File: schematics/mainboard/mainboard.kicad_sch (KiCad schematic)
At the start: 85 parts, among them J1 ICSP, J10 Conn_AGauge, J11 Conn_SAS, J2 USB_B_Micro, J3 DEALON DC-S050-200, J4 PWR_SELECT, J5 Conn_Joy1, J6 Conn_Joy2, J7 Conn_Throttle, J8 Conn_DGauges, J9 Conn_LCD, Q2 BC849, U1 ATmega2560-16A, U2 FT232RL, U3 USBLC6-2P6, U4 AIP78M05, U5 L9110, U6 74HC595, U7 74HC595, U8 74HC165, U9 74HC165, Y1 16Mhz

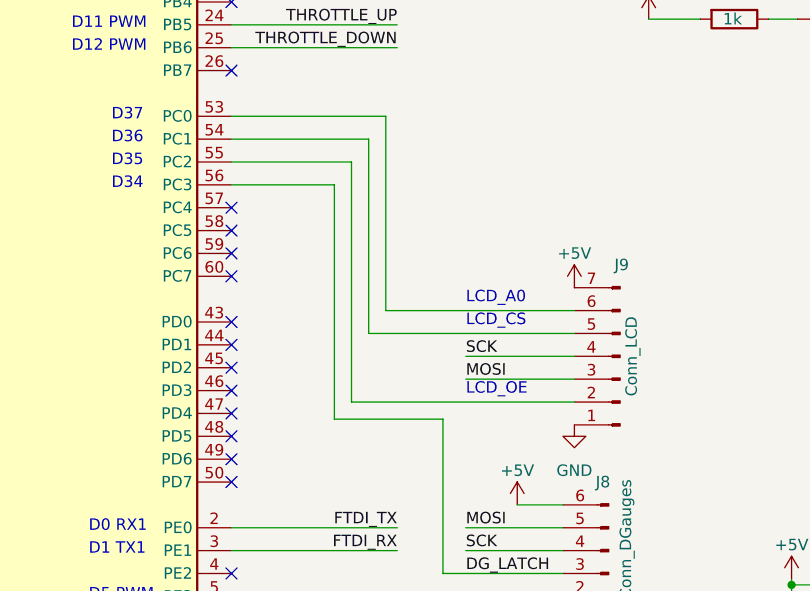
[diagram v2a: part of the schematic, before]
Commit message: SCH: LCD => removed MB OE connection, now pulled to 3.3, always ON
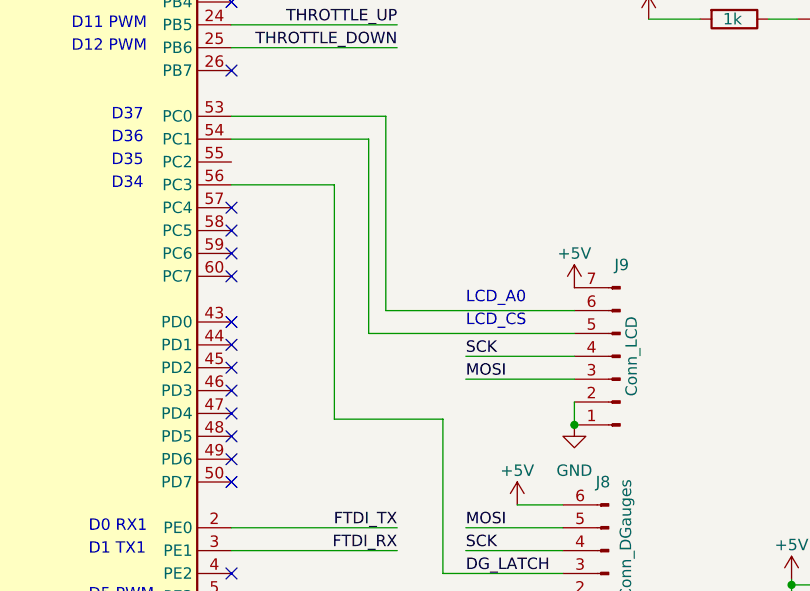
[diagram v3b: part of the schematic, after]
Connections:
- net GND: now also J9.2 (Pin_2)
- net at U1.55 (PC2): no longer J9.2 (Pin_2)
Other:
- note removed: "LCD_OE"
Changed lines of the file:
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@@
   (junction (at 245.745 269.24) (diameter 0) (color 0 0 0 0)
+  )
+  (junction (at 328.295 185.42) (diameter 0) (color 0 0 0 0)
   )
   (junction (at 341.63 218.44) (diameter 0) (color 0 0 0 0)
@@
     (stroke (width 0) (type default))
   )
+  (wire (pts (xy 328.295 182.88) (xy 328.295 185.42))
+    (stroke (width 0) (type default))
+  )
   (wire (pts (xy 290.195 140.97) (xy 308.61 140.97))
     (stroke (width 0) (type default))
@@
     (stroke (width 0) (type default))
   )
-  (wire (pts (xy 303.53 182.88) (xy 303.53 156.21))
-    (stroke (width 0) (type default))
-  )
   (wire (pts (xy 290.195 196.85) (xy 308.61 196.85))
     (stroke (width 0) (type default))
@@
     (stroke (width 0) (type default))
   )
-  (wire (pts (xy 303.53 156.21) (xy 290.195 156.21))
-    (stroke (width 0) (type default))
-  )
   (wire (pts (xy 129.54 147.32) (xy 129.54 146.05))
     (stroke (width 0) (type default))
@@
   )
   (wire (pts (xy 117.475 259.08) (xy 117.475 286.385))
-    (stroke (width 0) (type default))
-  )
-  (wire (pts (xy 303.53 182.88) (xy 328.295 182.88))
     (stroke (width 0) (type default))
   )
@@
     (effects (font (size 1.27 1.27)) (justify left bottom))
   )
-  (text "LCD_OE" (at 316.23 182.245 0)
-    (effects (font (size 1.27 1.27)) (justify left bottom))
-  )
